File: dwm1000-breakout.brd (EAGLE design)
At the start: 28.1 x 22.2 mm, 11 parts, among them U2 DWM1000

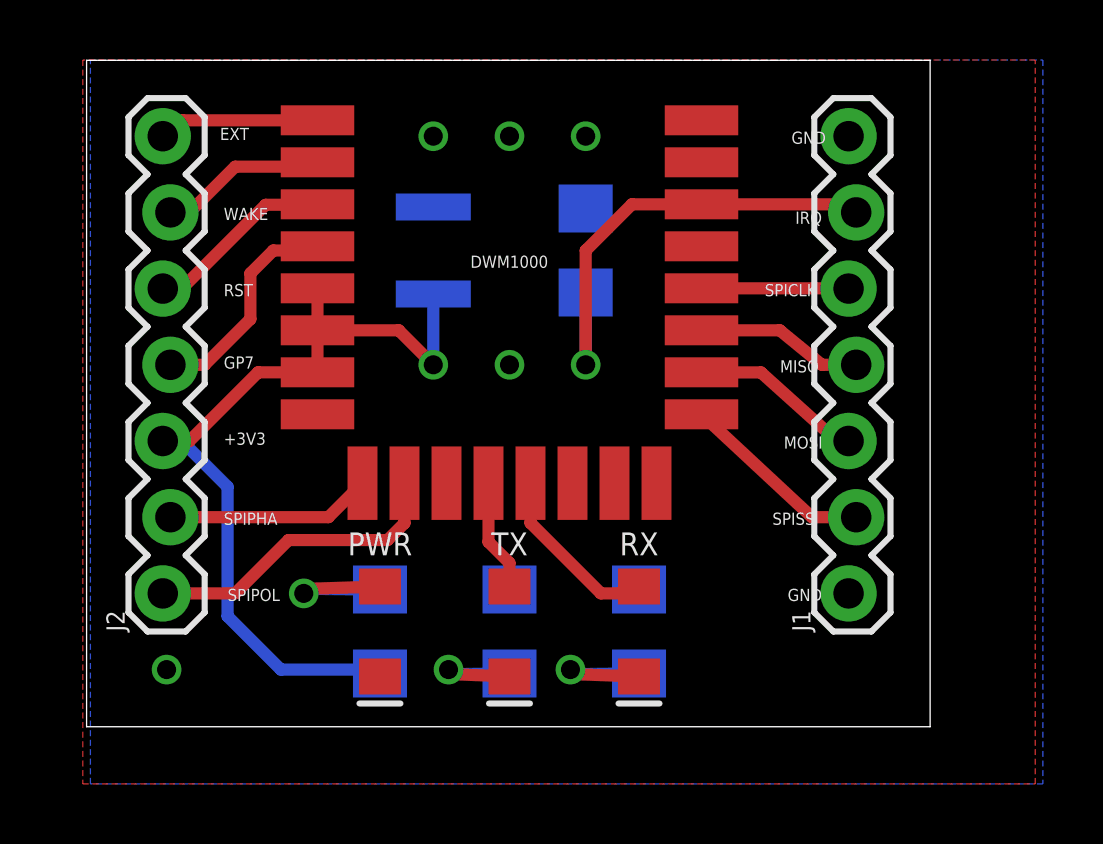
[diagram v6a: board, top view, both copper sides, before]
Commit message: Adding anchor board
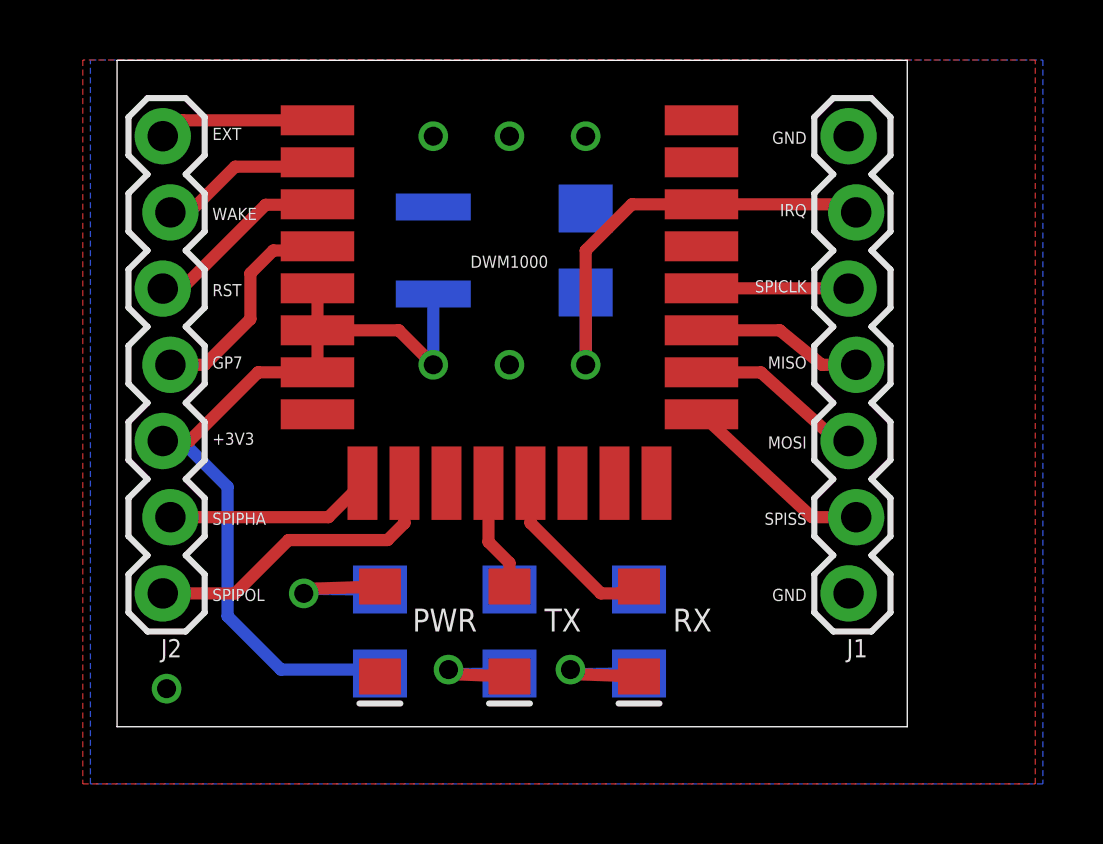
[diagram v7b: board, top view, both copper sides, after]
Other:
- board size 28.1 x 22.2 mm -> 26.3 x 22.2 mm
